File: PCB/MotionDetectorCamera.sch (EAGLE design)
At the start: 172 parts, among them J1 JUMPER-SOLDER, J12 JUMPER-AMPHENOL-10129380-9020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, J13 JUMPER-AMPHENOL-10129380-9020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, J14 JUMPER-AMPHENOL-10129380-9020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, J15 JUMPER-AMPHENOL-10129380-9020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, J2 JUMPER-SOLDER, J4 JUMPER-AMPHENOL-10129380-9020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, J5 JUMPER-SOLDER, J6 S-MOUNT-LENS-HOLDER, J7 MICROSD-SOCKET, J8 MINI-USB-JACK, Q10 PMOS-NEXPERIA-SOT1220, Q2 PMOS-NEXPERIA-SOT1220, Q3 PMOS-NEXPERIA-SOT1220, U1 NEXPERIA-74LVC1G98-BUFFER, U10 TI-TPS22919DCK, U11 TI-TPS2116, U12 TI-MSP430FR2422IRHL, U14 PANASONIC-EKMB110711X, U15 LATTICE-ICE40HX4K-BG121, U16 MICROCHIP-MCP7383X, U17 ON-AR0330CS1C12SPKA0, U18 ALLIANCE-AS4C8M16MSA-6BIN, U19 STM-STM32F730, U2 DIODESINC-AP7350, U20 DIODESINC-DT1446-04V-7, U21 NXP-NTB0102, U22 NXP-NTB0102, U23 TI-TPS6280XYKAR, U24 NEXPERIA-74LVC1G98-OR-INV-INP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, U28 NEXPERIA-74LVC1G98-NOR, U3 TI-TPS6280XYKAR, U30 TI-TPS22919DCK, U4 TI-TPS6280XYKAR, U5 WINBOND-W25Q40EW, U6 TI-TPS22919DCK, U7 TI-TPS22919DCK, U8 TI-TPS22919DCK, U9 TI-TPS22919DCK, X1 EPSON-FC-135, X2 SITIME-SIT8021, X3 SITIME-SIT8021

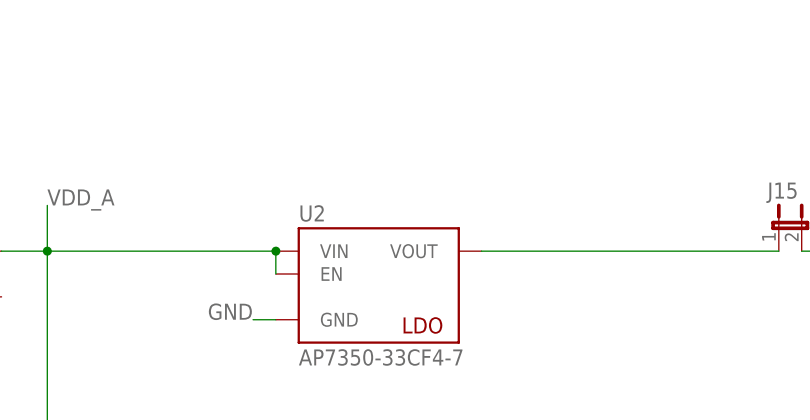
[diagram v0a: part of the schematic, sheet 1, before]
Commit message: Add reverse current blocking diode to LDO
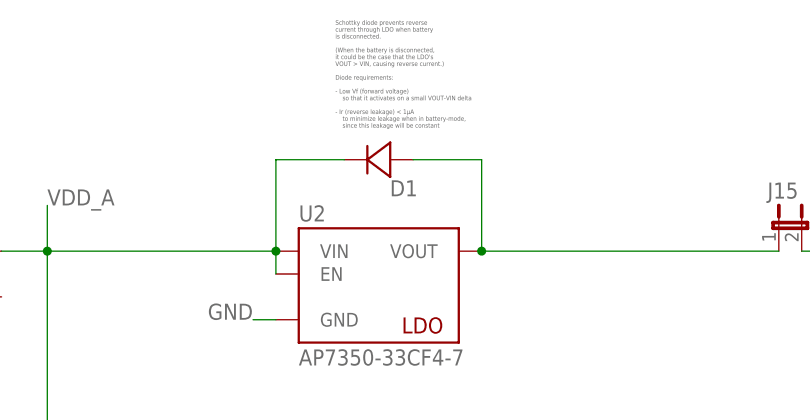
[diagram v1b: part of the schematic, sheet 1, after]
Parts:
- added D1: ROHM-RB168MM-40, EagleLibrary:ROHM-RB168MM-40
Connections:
- net N$3: now also D1.A
- net VDD_A: now also D1.C
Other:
- note added: "Schottky diode prevents reverse current through LDO when battery is disconnected. (When the battery is disconnected, it could be the case that the LDO's VOUT > VIN, causing reverse current.) Diode requirements: - Low Vf (forward voltage) so that it activates on a small VOUT-VIN delta - Ir (reverse leakage) < 1µA to minimize leakage when in battery-mode, since this leakage will be constant"
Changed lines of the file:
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@@
 <attribute name="PN" value="RC0402JR-0710KL"/>
 </part>
+<part name="D1" library="EagleLibrary" deviceset="ROHM-RB168MM-40" device=""/>
 </parts>
 <sheets>
@@
 <text x="213.106" y="207.01" size="1.27" layer="95" align="top-left">≤ 1%
 ≤ 200 ppm/°C </text>
+<text x="293.624" y="487.934" size="0.508" layer="95" align="top-left">Schottky diode prevents reverse
+current through LDO when battery
+is disconnected.
+(When the battery is disconnected,
+it could be the case that the LDO's
+VOUT &gt; VIN, causing reverse current.)
+Diode requirements:
+- Low Vf (forward voltage)
+    so that it activates on a small VOUT-VIN delta
+- Ir (reverse leakage) &lt; 1µA
+    to minimize leakage when in battery-mode,
+    since this leakage will be constant</text>
 </plain>
 <instances>
@@
 <attribute name="MFG" x="210.82" y="208.28" size="1.778" layer="96" rot="R90" display="off"/>
 <attribute name="PN" x="210.82" y="208.28" size="1.778" layer="96" rot="R90" display="off"/>
+</instance>
+<instance part="D1" gate="G$1" x="302.26" y="472.44" smashed="yes" rot="MR0">
+<attribute name="NAME" x="302.768" y="468.376" size="1.778" layer="95" rot="MR0"/>
 </instance>
 </instances>
@@
 <wire x1="294.64" y1="396.24" x2="261.62" y2="396.24" width="0.1524" layer="91"/>
 <wire x1="261.62" y1="462.28" x2="261.62" y2="396.24" width="0.1524" layer="91"/>
+<pinref part="D1" gate="G$1" pin="C"/>
+<wire x1="294.64" y1="472.44" x2="287.02" y2="472.44" width="0.1524" layer="91"/>
+<wire x1="287.02" y1="472.44" x2="287.02" y2="462.28" width="0.1524" layer="91"/>
 </segment>
 </net>
@@
 <wire x1="309.88" y1="462.28" x2="342.9" y2="462.28" width="0.1524" layer="91"/>
 <pinref part="U2" gate="G$1" pin="VOUT"/>
-</segment>
-</net>
+<wire x1="309.88" y1="462.28" x2="309.88" y2="472.44" width="0.1524" layer="91"/>
+<junction x="309.88" y="462.28"/>
+<pinref part="D1" gate="G$1" pin="A"/>
+<wire x1="309.88" y1="472.44" x2="302.26" y2="472.44" width="0.1524" layer="91"/>
+</segment>
+</net>

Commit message: Notes
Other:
- note added: "From W25Q40EWUXIE datasheet: "Note that the chip select pin (/CS) must track the VCC supply level at power-up until the VCC-min level and tVSL time delay is reached. If needed a pull-up resister on /CS can be used to accomplish this." We accomplish this because ICE40 has an internal pullup on its SPI_SS_B, which is connected to ICE_ST_SPI_CS_, so the output of the OR gate should be a high voltage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"
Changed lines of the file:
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@@
 small so they can be mounted
 below the chip.</text>
+<text x="72.644" y="-164.846" size="0.508" layer="95" align="top-left">From W25Q40EWUXIE datasheet:
+"Note that the chip select pin (/CS) must track the VCC
+supply level at power-up until the VCC-min level and
+tVSL time delay is reached. If needed a pull-up resister
+on /CS can be used to accomplish this."
+We accomplish this because ICE40 has an internal
+pullup on its SPI_SS_B, which is connected to
+ICE_ST_SPI_CS_, so the output of the OR gate
+should be a high voltage during power up.</text>
+<wire x1="76.2" y1="-162.56" x2="78.994" y2="-150.876" width="0.1524" layer="95"/>
 </plain>
 <instances>

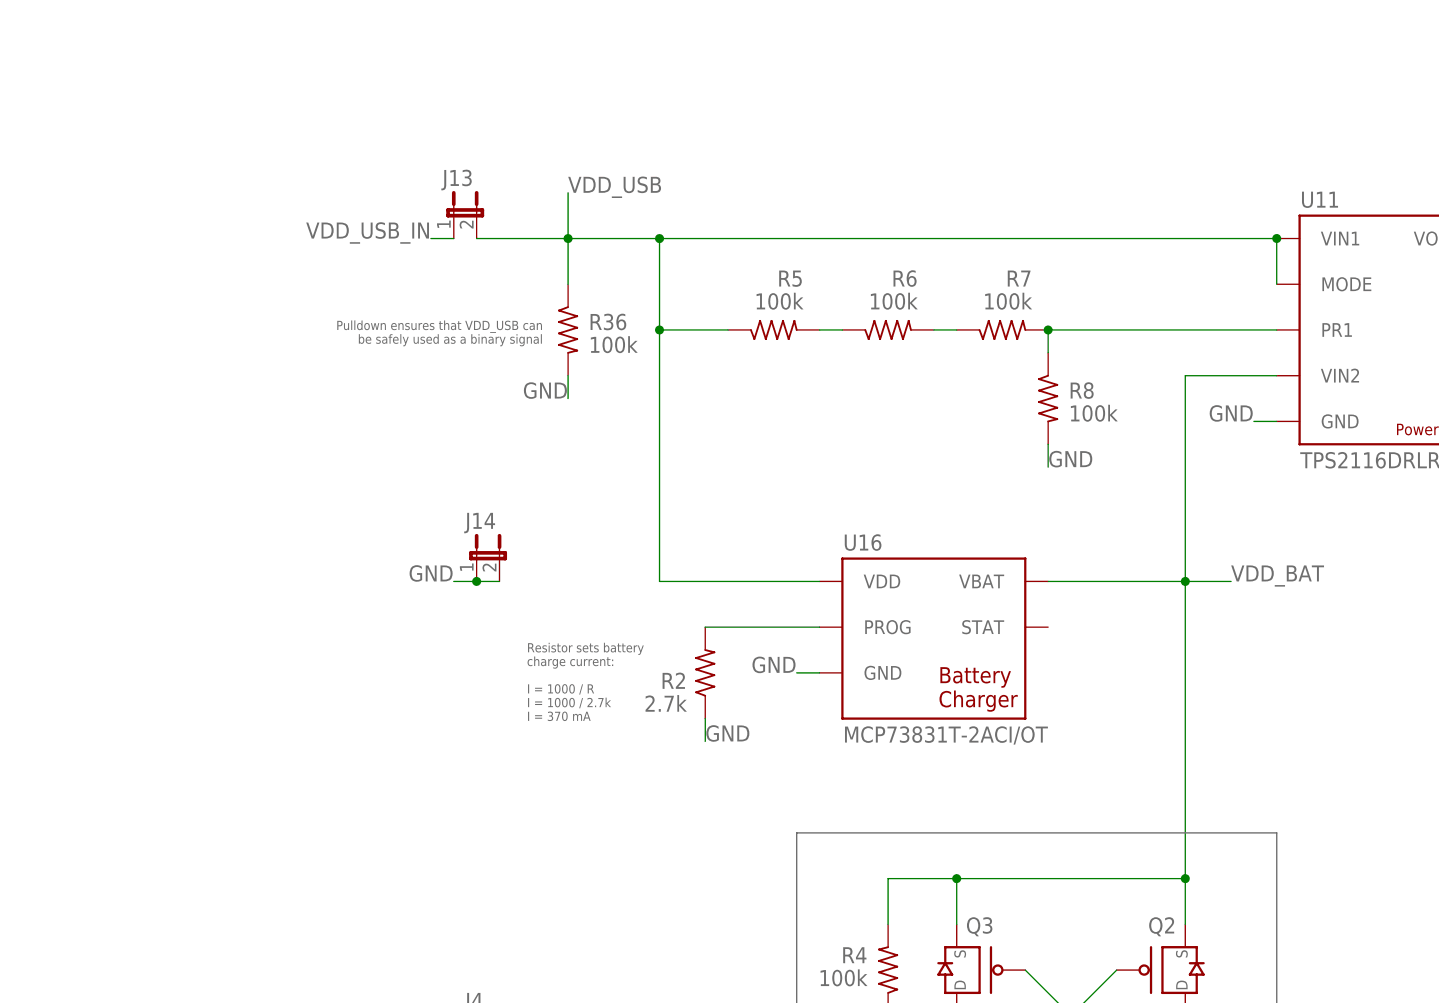
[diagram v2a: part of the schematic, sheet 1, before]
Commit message: Working on adding bypass capacitors
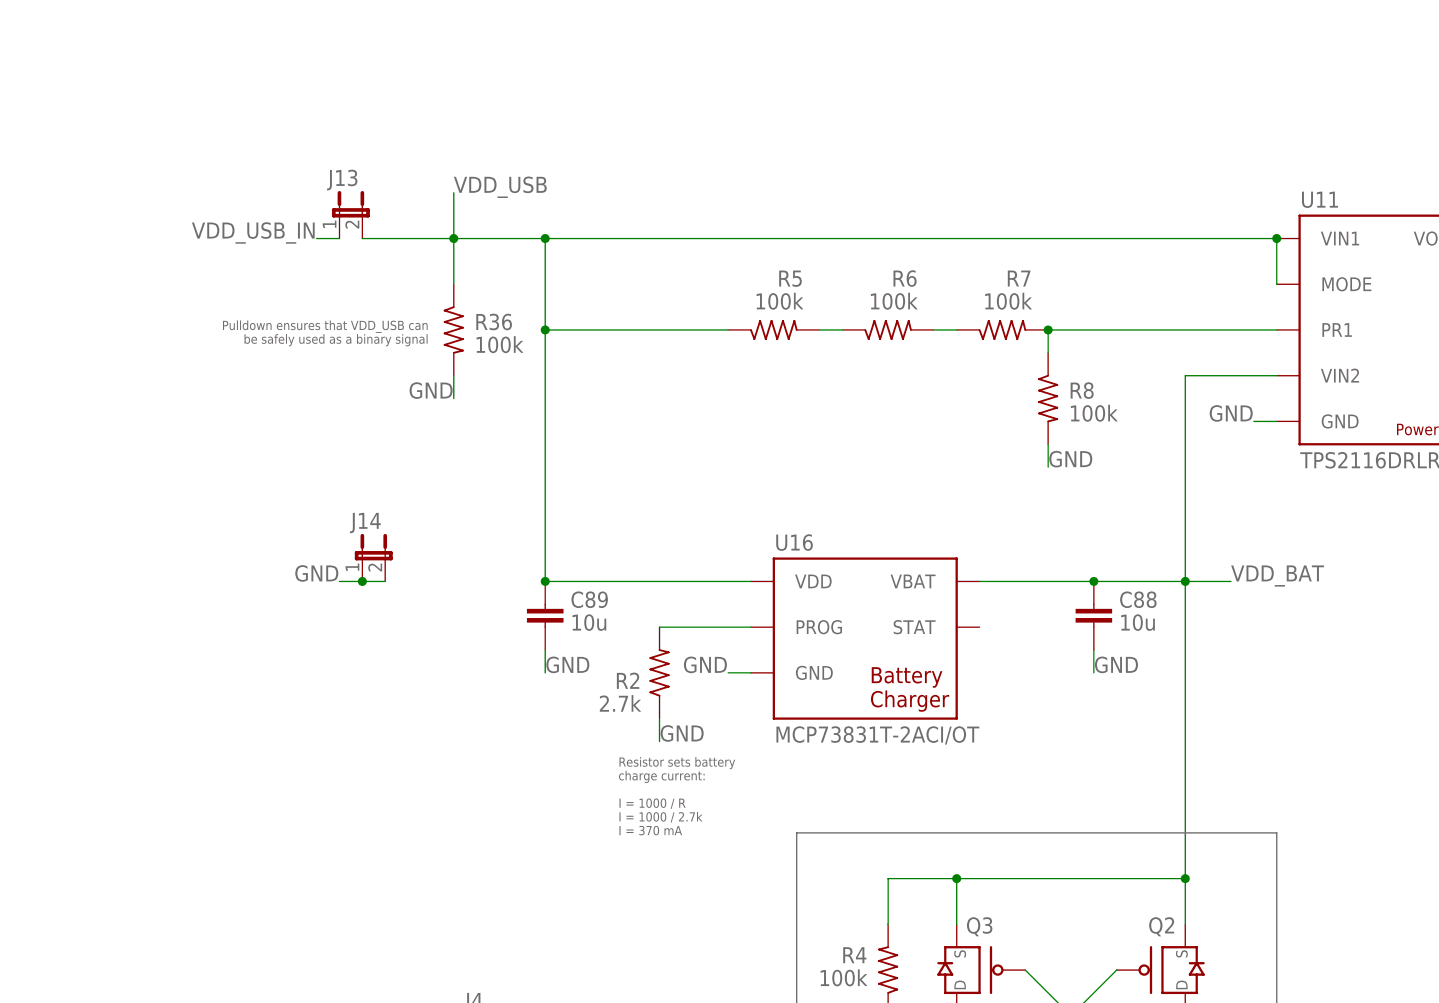
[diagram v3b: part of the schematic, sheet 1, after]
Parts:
- added C11, C12, C13, C14, C28: 100n, EagleLibrary:CAPACITOR0402
- added C88, C89: 10u, EagleLibrary:CAPACITOR0805
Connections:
- net GND: now also C11.2, C12.2, C13.2, C14.2, C28.2, C88.2, C89.2
- net VDD_A_3V3: now also C11.1, C12.1
- net VDD_BAT: now also C88.1
- net VDD_B_1V8: now also C14.1, C28.1
- net VDD_B_1V8_STM: now also C13.1
- net VDD_USB: now also C89.1
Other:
- moved on the sheet: J13, J14, R1, R2, R36, U16, U21, U22, U24

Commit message: Progress
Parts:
- added C90: 10u, EagleLibrary:CAPACITOR0805
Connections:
- net GND: now also C90.2
- net VDD_USB: now also C90.1
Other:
- moved on the sheet: C88, C89, J13, J14, J4, Q2, Q3, R2, R3, R4, U16

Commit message: Update notes
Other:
- note added: "Voltage divider sets VIN2 -> VIN1 switch voltage to 4V. That is, when VDD_USB reaches 4V, PR1=1V=VREF, so TPS2116 switches its VOUT to be sourced by VDD_USB."
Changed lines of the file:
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@@
     to minimize leakage when in battery-mode,
     since this leakage will be constant</text>
+<text x="178.816" y="448.056" size="1.016" layer="95" align="top-left">Voltage divider sets VIN2 -&gt; VIN1
+switch voltage to 4V.
+That is, when VDD_USB reaches 4V,
+PR1=1V=VREF, so TPS2116 switches
+its VOUT to be sourced by VDD_USB.</text>
 </plain>
 <instances>

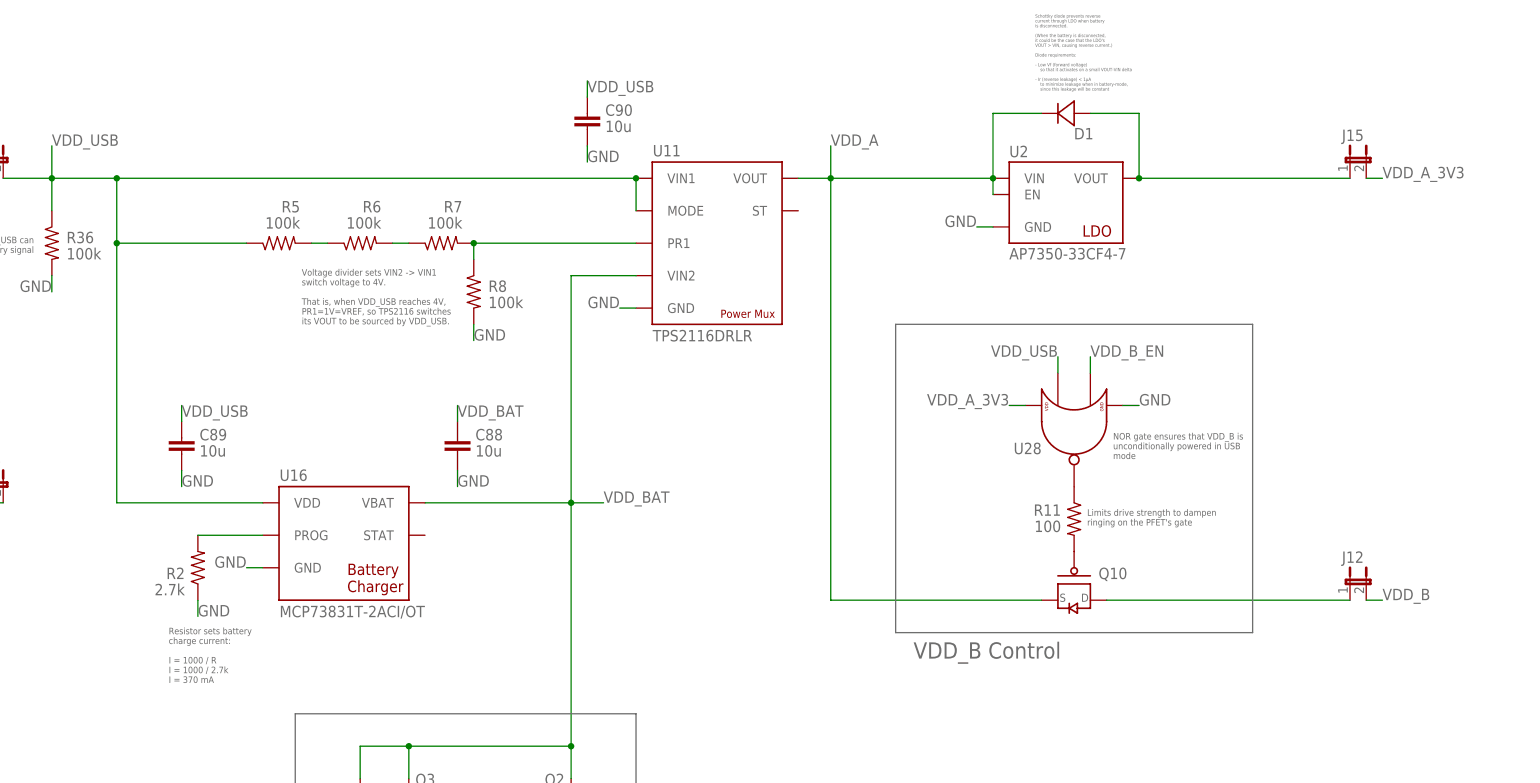
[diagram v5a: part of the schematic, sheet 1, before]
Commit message: Added bypass caps
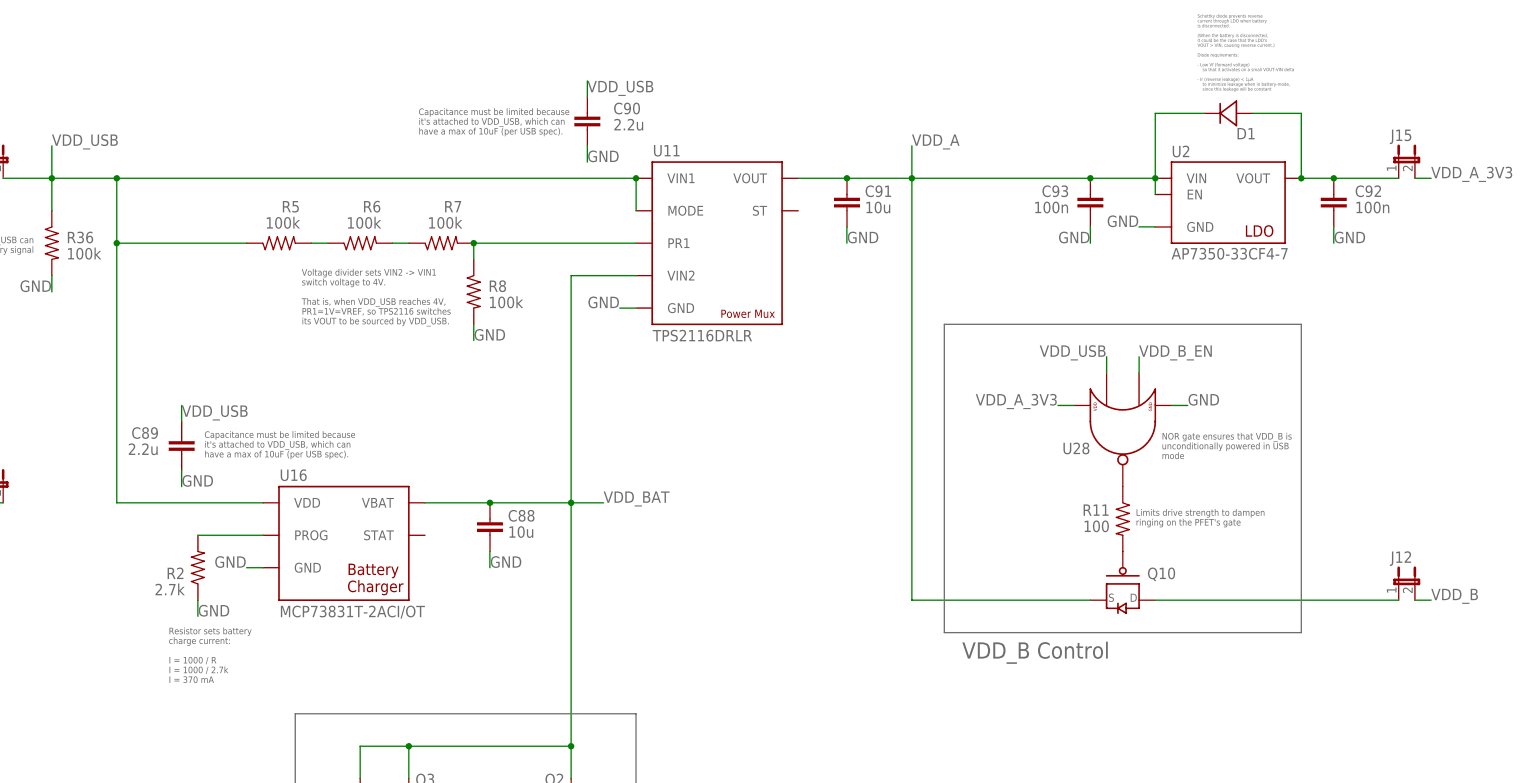
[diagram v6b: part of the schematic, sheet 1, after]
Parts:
- added C91: 10u, EagleLibrary:CAPACITOR0805
- added C92, C93: 100n, EagleLibrary:CAPACITOR0402
- C89, C90: value 10u -> 2.2u; device EagleLibrary:CAPACITOR0805 -> EagleLibrary:CAPACITOR0402; MFG Samsung -> Taiyo Yuden; PN CL21A106KOQNNNE -> TMK105CBJ225KV-F
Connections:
- net GND: now also C91.2, C92.2, C93.2
- net N$3: now also C92.1
- net VDD_A: now also C91.1, C93.1
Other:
- note added: "Capacitance must be limited because it's attached to VDD_USB, which can have a max of 10uF (per USB spec)."
- moved on the sheet: C88, D1, J12, J15, Q10, R11, U2, U28
